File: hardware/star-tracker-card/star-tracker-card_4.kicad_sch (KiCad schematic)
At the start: 22 parts, among them U1 RCLAMP0504FB, U7 OSD3358-512M-BSM, Y1 ECS-240-12-30BQ-AEN-TR, Y2 ABS07-32.768KHZ-T

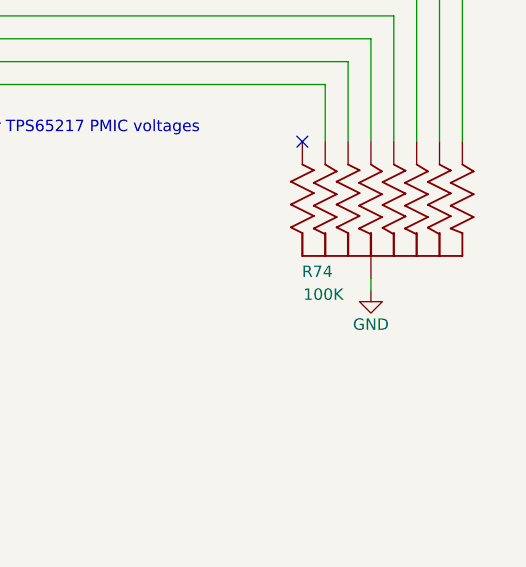
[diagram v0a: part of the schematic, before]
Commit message: Star Tracker v1.3 files, including new Makefile, Readme, and fixes in ERC, DRC, and layout
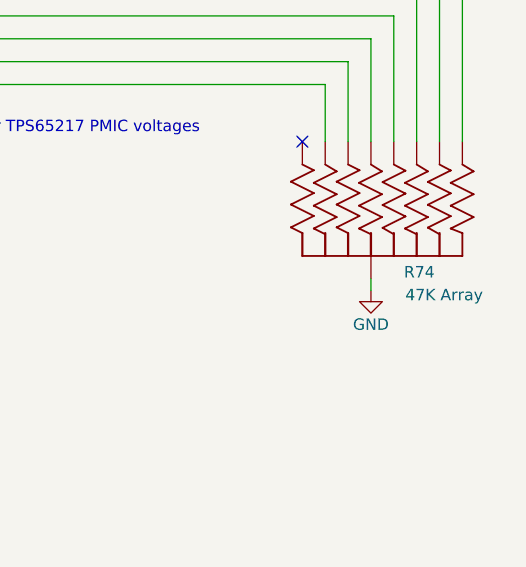
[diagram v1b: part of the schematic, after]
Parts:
- R74: value 100K -> 47K Array; DPN U7104CT-ND -> U7473CT-ND; MFR Panasonic Industry -> Panasonic Electronic Components; MPN EXB-A10P104J -> EXB-A10P473J
- Y1, Y2: DIS (none) -> DigiKey
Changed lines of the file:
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@@
 	(title_block
 		(title "OreSat Star Tracker")
-		(date "2026-04-15")
+		(date "2026-04-22")
 		(rev "1.3")
 		(company "Portland State Aerospace Society")
@@
 			)
 		)
+		(property "DIS" "DigiKey"
+			(at 152.4 60.96 90)
+			(hide yes)
+			(show_name no)
+			(do_not_autoplace no)
+			(effects
+				(font
+					(size 1.27 1.27)
+				)
+			)
+		)
 		(pin "1"
 		)
@@
 		(property "MPN" "ABS07-32.768KHZ-T"
 			(at 152.4 91.44 0)
+			(hide yes)
+			(show_name no)
+			(do_not_autoplace no)
+			(effects
+				(font
+					(size 1.27 1.27)
+				)
+			)
+		)
+		(property "DIS" "DigiKey"
+			(at 152.4 91.44 90)
 			(hide yes)
 			(show_name no)
@@
 		(dnp no)
 		(property "Reference" "R74"
-			(at 293.3192 138.3792 90)
+			(at 304.6476 138.43 90)
 			(show_name no)
 			(do_not_autoplace no)
@@
 			)
 		)
-		(property "Value" "100K"
-			(at 293.4716 140.9192 90)
+		(property "Value" "47K Array"
+			(at 304.8 140.97 90)
 			(show_name no)
 			(do_not_autoplace no)
@@
 			)
 		)
-		(property "Datasheet" "https://industrial.panasonic.com/ww/products/pt/resistor-network-array/models/EXBA10P104J"
+		(property "Datasheet" "http://www.vishay.com/docs/31509/csc.pdf"
 			(at 311.15 135.89 0)
 			(hide yes)
@@
 			)
 		)
-		(property "Description" "100k Ohm ±5% 62.5mW Power Per Element Bussed 8 Resistor Network/Array ±200ppm/°C 2512 (6432 Metric), Concave, Long Side Terminals"
+		(property "Description" "47k Ohm ±5% 62.5mW Power Per Element Bussed 8 Resistor Network/Array ±200ppm/°C 2512 (6432 Metric), Concave, Long Side Terminals"
 			(at 311.15 135.89 0)
 			(hide yes)
@@
 			)
 		)
-		(property "DPN" "U7104CT-ND"
+		(property "DPN" "U7473CT-ND"
 			(at 311.15 135.89 0)
 			(hide yes)
@@
 			)
 		)
-		(property "MPN" "EXB-A10P104J"
+		(property "MPN" "EXB-A10P473J"
 			(at 311.15 135.89 0)
 			(hide yes)
@@
 			)
 		)
-		(property "MFR" "Panasonic Industry"
+		(property "MFR" "Panasonic Electronic Components"
 			(at 311.15 135.89 90)
 			(hide yes)
